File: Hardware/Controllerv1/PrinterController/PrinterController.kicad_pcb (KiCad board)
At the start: 2 copper layers, 74 parts, among them J1 USB_B_Micro, J2 Conn_ARM_JTAG_SWD_10, J3 Conn_01x03, J4 Conn_01x03, J5 Screw_Terminal_01x08, Q1 Q_NMOS_DGS, Q2 Q_NMOS_DGS, Q3 Q_NMOS_DGS, Q4 Q_NMOS_DGS, Q5 Q_NMOS_DGS, Q6 Q_NMOS_DGS, U2 ZXGD3003E6, U3 ZXGD3003E6, U4 ZXGD3003E6, U5 ZXGD3003E6, U6 ZXGD3003E6, U7 ZXGD3003E6, Y1 12MHz, Y2 32.768

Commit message: Added updates to PCB
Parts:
- removed Q1, Q2, Q3, Q4: Q_NMOS_DGS, .pretty:SOT65P330X90-5N
- added J10: Conn_02x03_Odd_Even, Pin_Headers:Pin_Header_Straight_2x03_Pitch1.27mm_SMD, F.Cu at (49.6, 149.9)
- added J11: Conn_02x03_Odd_Even, Pin_Headers:Pin_Header_Straight_2x03_Pitch1.27mm_SMD, F.Cu at (43.9, 129.6)
- added J12: Conn_01x04, Socket_Strips:Socket_Strip_Straight_1x04_Pitch2.54mm, F.Cu at (33.7, 136.8)
- added J13: Conn_01x04, Socket_Strips:Socket_Strip_Straight_1x04_Pitch2.54mm, F.Cu at (33.5, 114.9)
- added J14: Conn_01x04, Socket_Strips:Socket_Strip_Straight_1x04_Pitch2.54mm, F.Cu at (35.4, 71.4)
- added J15: Conn_01x04, Socket_Strips:Socket_Strip_Straight_1x04_Pitch2.54mm, F.Cu at (33.9, 93.5)
- added J16: Conn_01x04, Socket_Strips:Socket_Strip_Straight_1x04_Pitch2.54mm, F.Cu at (69.5, 64.3)
- added J17: Conn_01x04, Socket_Strips:Socket_Strip_Straight_1x04_Pitch2.54mm, F.Cu at (106.2, 57.2)
- added J18: Conn_01x04, Socket_Strips:Socket_Strip_Straight_1x04_Pitch2.54mm, F.Cu at (76.8, 63.1)
- added J19: Conn_01x04, Socket_Strips:Socket_Strip_Straight_1x04_Pitch2.54mm, F.Cu at (91.6, 57.3)
- added J6: Conn_01x04, Socket_Strips:Socket_Strip_Straight_1x04_Pitch2.54mm, F.Cu at (56.6, 143.4)
- added J7: Conn_01x04, Socket_Strips:Socket_Strip_Straight_1x04_Pitch2.54mm, F.Cu at (56.6, 122.0)
- added J8: Conn_01x04, Socket_Strips:Socket_Strip_Straight_1x04_Pitch2.54mm, F.Cu at (56.6, 78.5)
- added J9: Conn_02x03_Odd_Even, Pin_Headers:Pin_Header_Straight_2x03_Pitch1.27mm_SMD, F.Cu at (43.9, 108.1)
- added U1: MCU-ATSAM3X8EA-AU-ND(LQFP144), MCU-ATSAM3X8EA-AU-ND_LQFP144_:LQFP144-0.5-20X20M, F.Cu at (73.9, 97.3)
- added U10: IRFR3711TRPBF, IRFR3711TRPBF:TO252, F.Cu at (107.5, 91.9)
- added U11: IRFR3711TRPBF, IRFR3711TRPBF:TO252, F.Cu at (107.5, 81.5)
- added U12: pololu_DRV8825, .pretty:DRV8825, F.Cu at (47.7, 140.4)
- added U13: pololu_DRV8825, .pretty:DRV8825, F.Cu at (47.7, 118.7)
- added U14: pololu_DRV8825, .pretty:DRV8825, F.Cu at (47.7, 75.5)
- added U15: pololu_DRV8825, .pretty:DRV8825, F.Cu at (47.7, 97.2)
- added U16: pololu_DRV8825, .pretty:DRV8825, F.Cu at (74.8, 63.7)
- added U17: pololu_DRV8825, .pretty:DRV8825, F.Cu at (94.2, 63.7)
- added U8: IRFR3711TRPBF, IRFR3711TRPBF:TO252, F.Cu at (107.5, 112.0)
- added U9: IRFR3711TRPBF, IRFR3711TRPBF:TO252, F.Cu at (107.5, 102.1)
- R10, R11, R12, R13, R14, R15, R16, R17, R18, R7, R8, R9, U2, U3, U4, U5, U6, U7: moved to B.Cu
- Y1: footprint Crystals:Crystal_HC52-8mm_Horizontal -> Crystals:Crystal_SMD_HC49-SD_HandSoldering
- Y2: footprint Crystals:Crystal_HC52-8mm_Horizontal -> Crystals:Crystal_SMD_MicroCrystal_CC7V-T1A-2pin_3.2x1.5mm_HandSoldering
- moved U7 150.6 mm to (89.0, 138.4)
- moved U6 150.3 mm to (89.2, 128.0)
- moved R18 150.1 mm to (93.7, 137.4)
- moved R17 149.7 mm to (93.7, 139.5)
- moved C32 149.4 mm to (95.6, 124.5)
- moved R16 149.0 mm to (94.6, 126.7)
- moved R15 148.6 mm to (94.6, 129.5)
- moved Q6 142.8 mm to (105.8, 137.7)
- moved Q5 142.4 mm to (105.8, 128.3)
- moved J4 140.5 mm to (114.6, 135.1)
- moved J3 140.4 mm to (114.6, 125.7)
- moved R8 135.6 mm to (93.3, 110.6)
- moved R14 135.6 mm to (93.3, 80.8)
- moved R12 135.6 mm to (93.3, 91.6)
- moved U5 135.4 mm to (89.5, 81.8)
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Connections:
- C27 pad 1: VDC -> +VDC
- C28 pad 1: VDC -> +VDC
- C29 pad 1: VDC -> +VDC
- C30 pad 1: VDC -> +VDC
- C31 pad 1: VDC -> +VDC
- C32 pad 1: VDC -> +VDC
- U2 pad 1: VDC -> +VDC
- U3 pad 1: VDC -> +VDC
- U4 pad 1: VDC -> +VDC
- U5 pad 1: VDC -> +VDC
- U6 pad 1: VDC -> +VDC
- U7 pad 1: VDC -> +VDC
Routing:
- net /Microcontroller/ZENABLE: track 0.00 -> 38.2 mm
- net +3V3: track 0.00 -> 34.0 mm
- net Net-(J9-Pad2): track 0.00 -> 26.5 mm
- net /Microcontroller/ZSTEP: track 0.00 -> 26.2 mm
- net Net-(J9-Pad6): track 0.00 -> 25.9 mm
- net Net-(J9-Pad4): track 0.00 -> 25.3 mm
- net Net-(J15-Pad4): track 0.00 -> 24.0 mm
- net Net-(J13-Pad4): track 0.00 -> 23.3 mm
- net Net-(J12-Pad4): track 0.00 -> 23.3 mm
- net Net-(J14-Pad4): track 0.00 -> 20.9 mm
- net Net-(J15-Pad3): track 0.00 -> 20.1 mm
- net Net-(J12-Pad3): track 0.00 -> 19.7 mm
- net Net-(J13-Pad3): track 0.00 -> 19.5 mm
- net Net-(J14-Pad3): track 0.00 -> 17.3 mm
- net Net-(J12-Pad2): track 0.00 -> 16.2 mm
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- added copper zone on F.Cu, net +VDC
- removed copper zone on F.Cu, net VDC
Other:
- board outline added: 246 x 110.2 mm
- rule trace_min: 0.2 -> 0.1524
- rule via_min_size: 0.4 -> 0.5

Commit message: Updated PCBS
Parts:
- added J22: Screw_Terminal_01x02, TerminalBlocks_WAGO:TerminalBlock_WAGO-804_RM7.5mm_2pol, F.Cu at (145.4, 29.6)
- added J23: Conn_01x03, Connectors_Molex:Molex_KK-6410-03_03x2.54mm_Straight, F.Cu at (167.3, 111.8)
- added J24: Screw_Terminal_01x02, TerminalBlocks_WAGO:TerminalBlock_WAGO-804_RM7.5mm_2pol, F.Cu at (130.8, 29.4)
- added JP1: Jumper_NO_Small, Resistors_SMD:R_0402, F.Cu at (-39.8, 126.5)
- added JP10: Jumper_NO_Small, Resistors_SMD:R_0402, F.Cu at (-12.5, 121.5)
- added JP11: Jumper_NO_Small, Resistors_SMD:R_0402, F.Cu at (-28.7, 172.6)
- added JP12: Jumper_NO_Small, Resistors_SMD:R_0402, F.Cu at (-28.7, 167.8)
- added JP13: Jumper_NO_Small, Resistors_SMD:R_0402, F.Cu at (-77.9, 146.4)
- added JP14: Jumper_NO_Small, Resistors_SMD:R_0402, F.Cu at (-20.7, 158.0)
- added JP15: Jumper_NO_Small, Resistors_SMD:R_0402, F.Cu at (-26.2, 126.5)
- added JP2: Jumper_NO_Small, Resistors_SMD:R_0402, F.Cu at (-39.8, 121.7)
- added JP3: Jumper_NO_Small, Resistors_SMD:R_0402, F.Cu at (-28.7, 162.9)
- added JP4: Jumper_NO_Small, Resistors_SMD:R_0402, F.Cu at (-20.7, 153.2)
- added JP5: Jumper_NO_Small, Resistors_SMD:R_0402, F.Cu at (-26.2, 121.7)
- added JP6: Jumper_NO_Small, Resistors_SMD:R_0402, F.Cu at (-15.1, 162.9)
- added JP7: Jumper_NO_Small, Resistors_SMD:R_0402, F.Cu at (-77.9, 156.1)
- added JP8: Jumper_NO_Small, Resistors_SMD:R_0402, F.Cu at (-77.9, 151.3)
- added JP9: Jumper_NO_Small, Resistors_SMD:R_0402, F.Cu at (-12.5, 126.3)
- J10, J11, J9: value Conn_02x03_Odd_Even -> Screw_Terminal_01x02; footprint Pin_Headers:Pin_Header_Straight_2x03_Pitch1.27mm_SMD -> TerminalBlocks_Phoenix:TerminalBlock_Phoenix_PT-3.5mm_2pol
- J12, J13, J14, J15, J16, J17: footprint Socket_Strips:Socket_Strip_Straight_1x04_Pitch2.54mm -> Connectors_Molex:Molex_KK-41791-04_04x3.96mm_Straight
- J5: value Screw_Terminal_01x08 -> Screw_Terminal_01x02; footprint TerminalBlocks_WAGO:TerminalBlock_WAGO-804_RM5mm_8pol -> TerminalBlocks_Phoenix:TerminalBlock_Phoenix_PT-3.5mm_2pol
- R10, R11, R12, R13, R14, R15, R16, R17, R18, R7, R8, R9, U2, U3, U4, U5, U6, U7: moved to F.Cu
- Y1: value 12MHz -> Crystal_GND24; footprint Crystals:Crystal_SMD_HC49-SD_HandSoldering -> Crystals:Crystal_SMD_3225-4pin_3.2x2.5mm_HandSoldering
- moved R14 176.3 mm to (252.3, 157.0), turned to 0 degrees
- moved J19 169.6 mm to (-40.3, 163.9)
- moved R11 167.7 mm to (248.7, 157.0), turned to 0 degrees
- moved J12 146.1 mm to (-68.8, 32.6)
- moved J16 143.4 mm to (-65.8, 17.0)
- moved U2 142.3 mm to (231.4, 105.2)
- moved U5 142.1 mm to (226.7, 118.9)
- moved J9 139.2 mm to (181.5, 129.1)
- moved J11 138.6 mm to (181.5, 112.5)
- moved C31 138.4 mm to (240.4, 118.8)
- moved Q6 137.7 mm to (241.9, 157.8)
- moved J8 135.3 mm to (-67.3, 132.7), turned to 0 degrees
- moved J10 135.0 mm to (181.5, 120.8), turned to 90 degrees
- moved J17 134.2 mm to (-22.0, 17.4)
- moved C21 129.5 mm to (217.8, 47.0)
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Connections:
- J10 pad 1: +3V3 -> /DriverStage/HEATER3_PWR
- J10 pad 2: Net-(J10-Pad2) -> GNDPWR
- J11 pad 1: +3V3 -> /DriverStage/HEATER4_PWR
- J11 pad 2: Net-(J11-Pad2) -> GNDPWR
- J9 pad 1: +3V3 -> /DriverStage/HEATER2_PWR
- J9 pad 2: Net-(J9-Pad2) -> GNDPWR
- U12 pad 16: +VDC -> VAA
- U12 pad 2: Net-(J10-Pad2) -> Net-(JP4-Pad2)
- U12 pad 3: Net-(J10-Pad4) -> Net-(JP5-Pad2)
- U12 pad 4: Net-(J10-Pad6) -> Net-(JP6-Pad2)
- U13 pad 16: +VDC -> VAA
- U13 pad 2: Net-(J11-Pad2) -> Net-(JP7-Pad2)
- U13 pad 3: Net-(J11-Pad4) -> Net-(JP8-Pad2)
- U13 pad 4: Net-(J11-Pad6) -> Net-(JP9-Pad2)
- U14 pad 16: +VDC -> VAA
- U14 pad 2: Net-(J9-Pad2) -> Net-(JP1-Pad2)
- U14 pad 3: Net-(J9-Pad4) -> Net-(JP2-Pad2)
- U14 pad 4: Net-(J9-Pad6) -> Net-(JP3-Pad2)
- U15 pad 16: +VDC -> VAA
- U15 pad 2: Net-(J9-Pad2) -> Net-(JP1-Pad2)
- U15 pad 3: Net-(J9-Pad4) -> Net-(JP2-Pad2)
- U15 pad 4: Net-(J9-Pad6) -> Net-(JP3-Pad2)
- U16 pad 16: +VDC -> VAA
- U17 pad 16: +VDC -> VAA
- Y1 pad 2: Net-(C2-Pad1) -> GND
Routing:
- net /Microcontroller/ZENABLE: track 38.2 -> 0.00 mm
- net +3V3: track 34.0 -> 0.00 mm
- net Net-(J9-Pad2): track 26.5 -> 0.00 mm
- net /Microcontroller/ZSTEP: track 26.2 -> 0.00 mm
- net Net-(J9-Pad6): track 25.9 -> 0.00 mm
- net Net-(J9-Pad4): track 25.3 -> 0.00 mm
- net Net-(J15-Pad4): track 24.0 -> 0.00 mm
- net Net-(J13-Pad4): track 23.3 -> 0.00 mm
- net Net-(J12-Pad4): track 23.3 -> 0.00 mm
- net Net-(J14-Pad4): track 20.9 -> 0.00 mm
- net Net-(J15-Pad3): track 20.1 -> 0.00 mm
- net Net-(J12-Pad3): track 19.7 -> 0.00 mm
- net Net-(J13-Pad3): track 19.5 -> 0.00 mm
- net Net-(J14-Pad3): track 17.3 -> 0.00 mm
- net Net-(J12-Pad2): track 16.2 -> 0.00 mm
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- removed copper zone on F.Cu, net +VDC
- removed copper zone on F.Cu, net /DriverStage/HEATER1_PWR
- removed copper zone on F.Cu, net /DriverStage/HEATER2_PWR
- removed copper zone on F.Cu, net /DriverStage/HEATER3_PWR
- removed copper zone on F.Cu, net /DriverStage/HEATER4_PWR
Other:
- board size 246 x 110.2 mm -> 87.6 x 124.9 mm

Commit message: Added routed Power switching circuitry
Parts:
- removed JP10, JP11, JP12, JP13, JP14, JP15, JP3, JP4, JP5, JP6, JP7, JP8, JP9: Jumper_NO_Small, Resistors_SMD:R_0402
- removed R16, R18: 10k, Resistors_SMD:R_0805
- removed U12, U14, U15, U16, U17: pololu_DRV8825, .pretty:DRV8825
- removed U7: ZXGD3003E6, TO_SOT_Packages_SMD:SOT-23-6
- added C34: 100u, Capacitors_Tantalum_SMD:CP_Tantalum_Case-D_EIA-7343-31_Hand, F.Cu at (161.1, 136.2)
- added C35: 470u, Capacitors_Tantalum_SMD:CP_Tantalum_Case-D_EIA-7343-31_Hand, F.Cu at (172.1, 136.2)
- added C36: 100u, Capacitors_Tantalum_SMD:CP_Tantalum_Case-B_EIA-3528-21_Hand, F.Cu at (172.1, 119.6)
- added C38: 100u, Capacitors_Tantalum_SMD:CP_Tantalum_Case-D_EIA-7343-31_Hand, F.Cu at (142.8, 136.2)
- added C39: 470u, Capacitors_Tantalum_SMD:CP_Tantalum_Case-D_EIA-7343-31_Hand, F.Cu at (154.3, 136.2)
- added C40: 100u, Capacitors_Tantalum_SMD:CP_Tantalum_Case-B_EIA-3528-21_Hand, F.Cu at (154.3, 119.2)
- added D4: D, Diodes_SMD:D_SOD-123, F.Cu at (221.2, 135.0)
- added D5: D, Diodes_SMD:D_SOD-123, F.Cu at (221.2, 132.5)
- added J20: Conn_01x02, Connectors_Molex:Molex_KK-6410-02_02x2.54mm_Straight, F.Cu at (144.6, 86.0)
- added J21: USB_OTG, Connectors_USB:USB_Micro-B_Molex-105017-0001, F.Cu at (141.0, 100.4)
- added J25: Conn_ARM_JTAG_SWD_10, Connectors_Harwin:Harwin_Gecko-G125-FVX1005L0X_2x05x1.25mm_Straight, F.Cu at (218.0, 99.5)
- added L6: 1u, Capacitors_SMD:C_0805, F.Cu at (172.1, 126.4)
- added L8: 1u, Capacitors_SMD:C_0805, F.Cu at (154.3, 126.6)
- added R25: 100K, Resistors_SMD:R_0805, F.Cu at (165.8, 78.5)
- added R26: 100K, Resistors_SMD:R_0805, F.Cu at (169.0, 76.6)
- added R27: 100K, Resistors_SMD:R_0805, F.Cu at (165.8, 76.6)
- D1: footprint LEDs:LED_0805 -> Capacitors_Tantalum_SMD:CP_Tantalum_Case-B_EIA-3528-21_Hand
- J1: value USB_B_Micro -> Conn_01x03; footprint Connectors:USB_Micro-B_10103594-0001LF -> Connectors_Molex:Molex_KK-6410-03_03x2.54mm_Straight
- J12, J13, J14, J15: value Conn_01x04 -> Conn_01x03; footprint Connectors_Molex:Molex_KK-41791-04_04x3.96mm_Straight -> Connectors_Molex:Molex_KK-6410-03_03x2.54mm_Straight
- J16, J17: value Conn_01x04 -> Conn_01x02; footprint Connectors_Molex:Molex_KK-41791-04_04x3.96mm_Straight -> Connectors_Molex:Molex_KK-6410-02_02x2.54mm_Straight
- J18, J19, J6, J7, J8: footprint Socket_Strips:Socket_Strip_Straight_1x04_Pitch2.54mm -> Connectors_Molex:Molex_KK-6410-04_04x2.54mm_Straight
- J2: value Conn_ARM_JTAG_SWD_10 -> Conn_01x03; footprint Pin_Headers:Pin_Header_Straight_2x05_Pitch1.27mm -> Connectors_Molex:Molex_KK-6410-03_03x2.54mm_Straight
- JP1, JP2: value Jumper_NO_Small -> Jumper_NC_Small; footprint Resistors_SMD:R_0402 -> Pin_Headers:Pin_Header_Straight_1x02_Pitch2.54mm
- R10, R11, R12, R13, R14, R7, R8, R9, U2, U3, U4, U5: moved to B.Cu
- U1: value MCU-ATSAM3X8EA-AU-ND(LQFP144) -> R-78E5.0-1.0; footprint MCU-ATSAM3X8EA-AU-ND_LQFP144_:LQFP144-0.5-20X20M -> Converters_DCDC_ACDC:DCDC-Conv_RECOM_R-78E-0.5
- U13: value pololu_DRV8825 -> MCU-ATSAM3X8EA-AU-ND(LQFP144); footprint .pretty:DRV8825 -> MCU-ATSAM3X8EA-AU-ND_LQFP144_:LQFP144-0.5-20X20M
- U6: value ZXGD3003E6 -> R-78E3.3-1.0; footprint TO_SOT_Packages_SMD:SOT-23-6 -> Converters_DCDC_ACDC:DCDC-Conv_RECOM_R-78E-0.5
- moved J12 306.3 mm to (231.7, 92.2)
- moved J14 302.9 mm to (231.7, 85.1)
- moved J13 300.5 mm to (231.7, 70.9)
- moved J15 286.5 mm to (231.7, 99.8)
- moved J19 275.4 mm to (216.4, 64.1)
- moved JP2 270.9 mm to (230.5, 140.0), turned to 180 degrees
- moved J8 269.7 mm to (193.5, 64.1)
- moved JP1 267.1 mm to (227.0, 140.0), turned to 180 degrees
- moved J16 222.6 mm to (144.6, 89.8), turned to 270 degrees
- moved J18 213.5 mm to (205.0, 64.1)
- moved J7 209.6 mm to (182.1, 64.1)
- moved U13 208.7 mm to (194.6, 91.3), turned to 270 degrees
- moved J6 207.8 mm to (170.7, 64.1)
- moved J17 177.8 mm to (144.6, 79.7), turned to 90 degrees
- moved J1 128.4 mm to (231.7, 63.8), turned to 0 degrees
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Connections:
- C27 pad 2: GND -> GNDPWR
- C28 pad 2: GND -> GNDPWR
- C29 pad 2: GND -> GNDPWR
- C30 pad 2: GND -> GNDPWR
- C31 pad 1: +VDC -> Net-(C31-Pad1)
- C31 pad 2: GND -> GNDPWR
- C32 pad 1: +VDC -> Net-(C31-Pad1)
- C32 pad 2: GND -> GNDPWR
- J1 pad 1: VBUS -> GND
- J1 pad 2: Net-(J1-Pad2) -> +3V3
- J1 pad 3: Net-(J1-Pad3) -> /Motor Connections/ESX1
- J12 pad 1: Net-(J12-Pad1) -> GND
- J12 pad 2: Net-(J12-Pad2) -> +3V3
- J12 pad 3: Net-(J12-Pad3) -> /Motor Connections/ESZ1
- J13 pad 1: Net-(J13-Pad1) -> GND
- J13 pad 2: Net-(J13-Pad2) -> +3V3
- J13 pad 3: Net-(J13-Pad3) -> /Motor Connections/ESX2
- J14 pad 1: Net-(J14-Pad1) -> GND
- J14 pad 2: Net-(J14-Pad2) -> +3V3
- J14 pad 3: Net-(J14-Pad3) -> /Motor Connections/ESY2
- J15 pad 1: Net-(J15-Pad1) -> GND
- J15 pad 2: Net-(J15-Pad2) -> +3V3
- J15 pad 3: Net-(J15-Pad3) -> /Motor Connections/ESZ2
- J16 pad 1: Net-(J16-Pad1) -> /Microcontroller/TEMP1
- J16 pad 2: Net-(J16-Pad2) -> +3V3
- J17 pad 1: Net-(J17-Pad1) -> /Microcontroller/TEMP2
- J17 pad 2: Net-(J17-Pad2) -> +3V3
- J2 pad 1: +3V3 -> GND
- J2 pad 2: Net-(J2-Pad2) -> +3V3
- J2 pad 3: GND -> /Motor Connections/ESY1
- J3 pad 1: +VDC -> Net-(C31-Pad1)
- J4 pad 1: +VDC -> Net-(C31-Pad1)
- J6 pad 1: /Microcontroller/XDIR -> /Microcontroller/XENABLE
- J6 pad 3: /Microcontroller/XENABLE -> /Microcontroller/XDIR
- J7 pad 1: /Microcontroller/YDIR -> /Microcontroller/YENABLE
- J7 pad 3: /Microcontroller/YENABLE -> /Microcontroller/YDIR
- J8 pad 1: /Microcontroller/ZDIR -> /Microcontroller/ZENABLE
- J8 pad 3: /Microcontroller/ZENABLE -> /Microcontroller/ZDIR
- JP1 pad 1: +3V3 -> Net-(C31-Pad1)
- JP2 pad 1: +3V3 -> Net-(C31-Pad1)
- Q5 pad 1: +VDC -> Net-(C31-Pad1)
- Q6 pad 1: +VDC -> Net-(C31-Pad1)
- R15 pad 2: Net-(R15-Pad2) -> /DriverStage/FAN1
- R17 pad 2: Net-(R17-Pad2) -> /DriverStage/FAN2
- R2 pad 2: Net-(J1-Pad2) -> Net-(J21-Pad2)
- R3 pad 2: Net-(J1-Pad3) -> Net-(J21-Pad3)
- U1 pad 1: /Microcontroller/XMIN -> VAA
- U1 pad 2: Net-(U1-Pad2) -> GNDPWR
- U13 pad 1: /Microcontroller/YENABLE -> /Motor Connections/ESX1
- U13 pad 10: Net-(U13-Pad10) -> VDD
- U13 pad 11: Net-(J13-Pad4) -> (no net)
- U13 pad 12: Net-(J13-Pad3) -> Net-(U13-Pad12)
- U13 pad 13: Net-(J13-Pad2) -> (no net)
- U13 pad 14: Net-(J13-Pad1) -> /Motor Connections/ESZ1
- U13 pad 15: GND -> (no net)
- U13 pad 16: VAA -> /Microcontroller/E0DIR
- U13 pad 2: Net-(JP7-Pad2) -> (no net)
- U13 pad 3: Net-(JP8-Pad2) -> (no net)
- U13 pad 4: Net-(JP9-Pad2) -> (no net)
- U13 pad 5: +3V3 -> (no net)
- U13 pad 6: +3V3 -> (no net)
- U13 pad 7: /Microcontroller/YSTEP -> (no net)
- U13 pad 8: /Microcontroller/YDIR -> /Motor Connections/ESY1
- U13 pad 9: GND -> (no net)
- U2 pad 3: GND -> GNDPWR
- U2 pad 5: Net-(U2-Pad5) -> (no net)
- U3 pad 3: GND -> GNDPWR
- U3 pad 5: Net-(U3-Pad5) -> (no net)
- U4 pad 3: GND -> GNDPWR
- U4 pad 5: Net-(U4-Pad5) -> (no net)
- U5 pad 3: GND -> GNDPWR
- U5 pad 5: Net-(U5-Pad5) -> (no net)
- U6 pad 1: +VDC -> VAA
- U6 pad 2: /DriverStage/FAN1 -> GNDPWR
- U6 pad 3: GND -> Net-(C39-Pad1)
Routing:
- net +VDC: track 0.00 -> 80.1 mm, vias 0 -> 4
- net +5V: track 0.00 -> 54.0 mm
- net Net-(C31-Pad1): track 0.00 -> 40.5 mm
- net /DriverStage/FAN1: track 0.00 -> 26.1 mm, vias 0 -> 1
- net /DriverStage/FAN2: track 0.00 -> 24.7 mm, vias 0 -> 1
- net +3V3: track 0.00 -> 17.0 mm
- net /DriverStage/HEATER1: track 0.00 -> 15.8 mm
- net /DriverStage/HEATER2: track 0.00 -> 15.4 mm
- net Net-(C39-Pad1): track 0.00 -> 15.1 mm
- net Net-(C35-Pad1): track 0.00 -> 14.9 mm
- net /DriverStage/HEATER3: track 0.00 -> 14.7 mm
- net /DriverStage/HEATER4: track 0.00 -> 14.3 mm
- net Net-(C1-Pad1): track 12.2 -> 0.00 mm
- net Net-(D5-Pad1): track 0.00 -> 11.8 mm
- net /DriverStage/HEATER4_PWR: track 0.00 -> 9.31 mm
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- added copper zone on F.Cu, net +VDC
- added copper zone on B.Cu, net GNDPWR
- added copper zone on F.Cu, net GNDPWR
- added copper zone on F.Cu, net VAA
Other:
- board size 87.6 x 124.9 mm -> 100 x 100 mm

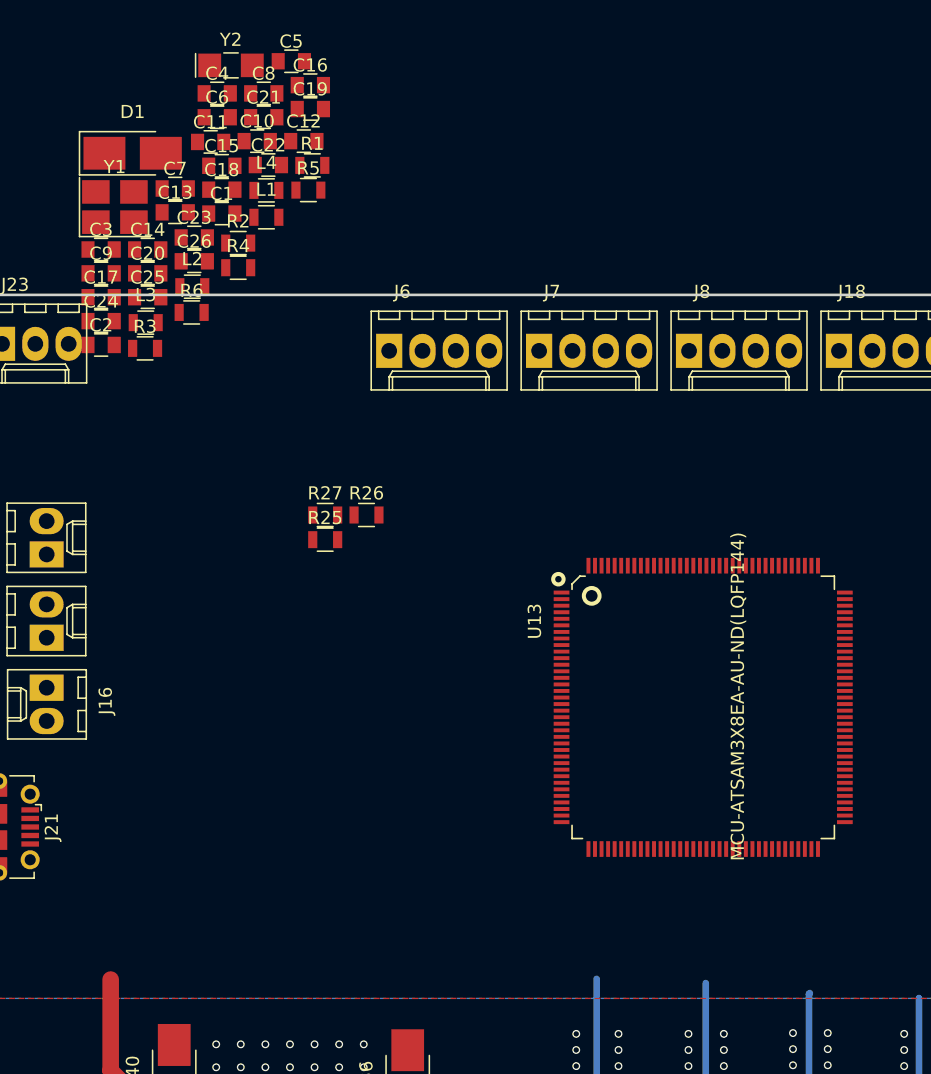
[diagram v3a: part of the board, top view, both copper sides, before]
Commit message: Added additional PCB layout
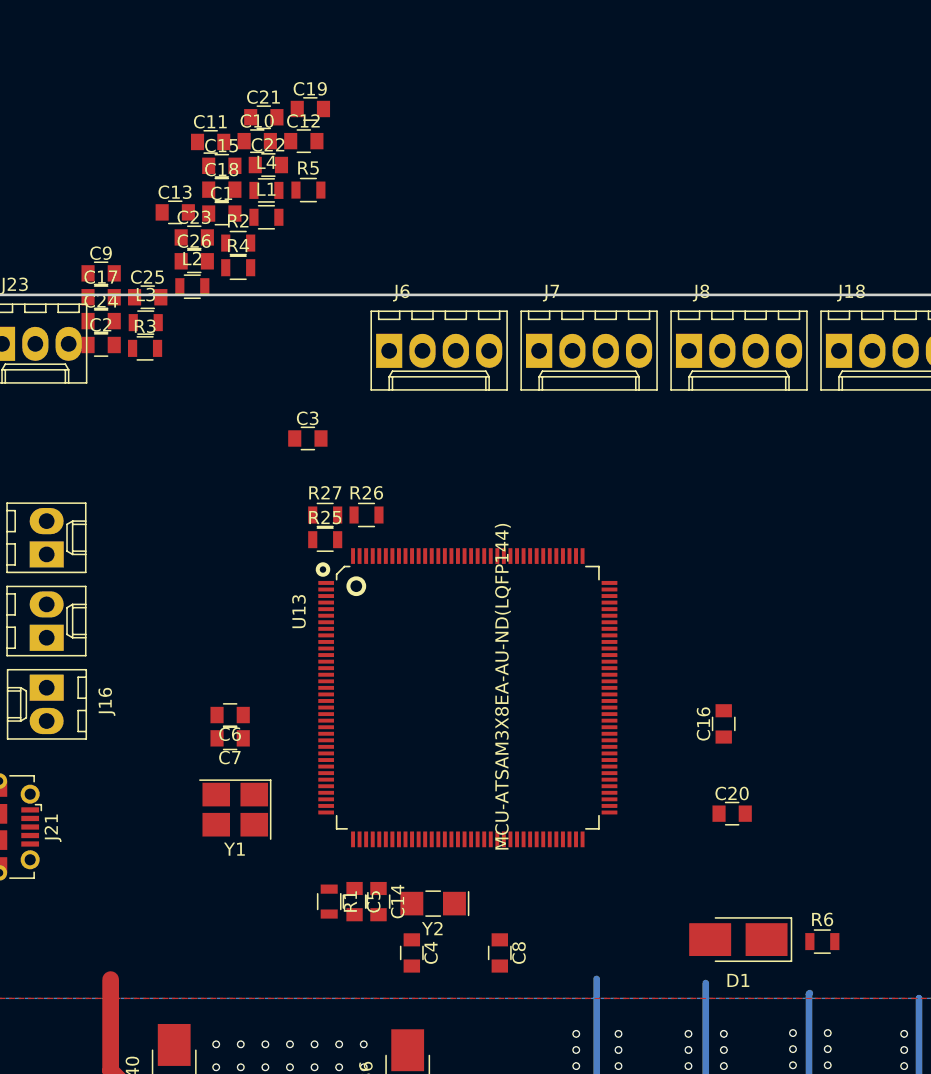
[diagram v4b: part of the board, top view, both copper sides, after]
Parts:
- C1, C2, C3, C4: value C -> 22p
- moved D1 75.7 mm to (197.3, 109.0), turned to 180 degrees
- moved C8 68.0 mm to (179.1, 110.0), turned to 270 degrees
- moved R6 67.9 mm to (203.7, 109.2)
- moved C4 67.2 mm to (172.4, 110.0), turned to 270 degrees
- moved Y2 65.7 mm to (174.0, 106.3), turned to 180 degrees
- moved C5 64.2 mm to (168.0, 106.1), turned to 270 degrees
- moved C20 60.7 mm to (196.8, 99.4)
- moved C16 58.0 mm to (196.2, 92.6), turned to 90 degrees
- moved R1 56.1 mm to (166.1, 106.1), turned to 270 degrees
- moved C14 52.7 mm to (169.9, 106.1), turned to 270 degrees
- moved Y1 46.8 mm to (159.0, 99.1), turned to 180 degrees
- moved C6 45.6 mm to (158.6, 91.9), turned to 180 degrees
- moved C7 42.1 mm to (158.6, 93.7), turned to 180 degrees
- moved C3 21.4 mm to (164.5, 70.8)
- moved U13 18.0 mm to (176.7, 90.6)

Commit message: Added Motor driver revision 1.0
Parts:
- moved C9 70.7 mm to (207.9, 97.0)
- moved L4 68.1 mm to (201.9, 106.6), turned to 270 degrees
- moved C10 66.6 mm to (207.9, 95.1)
- moved C18 64.8 mm to (207.9, 93.2)
- moved C24 64.5 mm to (207.9, 87.6)
- moved C19 61.5 mm to (207.9, 89.5)
- moved C15 59.8 mm to (184.3, 103.7), turned to 270 degrees
- moved C13 59.3 mm to (186.1, 103.7), turned to 270 degrees
- moved C22 58.6 mm to (207.9, 85.7)
- moved Y1 50.6 mm to (209.4, 102.2), turned to 90 degrees
- moved C7 48.9 mm to (205.7, 106.6), turned to 270 degrees
- moved C6 47.7 mm to (203.9, 106.6), turned to 270 degrees
- moved C21 41.9 mm to (172.1, 86.8), turned to 180 degrees
- moved R3 36.7 mm to (188.1, 56.8)
- moved C25 34.8 mm to (172.1, 88.6), turned to 180 degrees
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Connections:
- C11 pad 1: /Microcontroller/VDDHMI -> /Microcontroller/VDDMI
- C14 pad 1: /Microcontroller/VDDHMI -> /Microcontroller/VDDMI
- U13 pad 104: (no net) -> VDD
- U13 pad 105: (no net) -> +3V3
- U13 pad 106: (no net) -> GND
- U13 pad 11: (no net) -> +3V3
- U13 pad 12: Net-(U13-Pad12) -> GND
- U13 pad 124: (no net) -> VDD
- U13 pad 125: (no net) -> +3V3
- U13 pad 33: (no net) -> GND
- U13 pad 44: Net-(U13-Pad12) -> GND
- U13 pad 45: (no net) -> VDD
- U13 pad 54: (no net) -> GND
- U13 pad 58: (no net) -> GND
- U13 pad 61: (no net) -> VDD
- U13 pad 62: (no net) -> +3V3
- U13 pad 74: (no net) -> GND
